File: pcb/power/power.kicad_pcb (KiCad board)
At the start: 4 copper layers, 100 x 100 mm, 34 parts, among them J101 XT30PW-M, J102 Conn_02x10_Row_Letter_First, U201 TPS62933, U301 INA226, U401 INA226

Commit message: update ALL parts
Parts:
- C102, C103: footprint Capacitor_Tantalum_SMD:CP_EIA-7343-43_Kemet-X_Pad2.25x2.55mm_HandSolder -> Capacitor_Tantalum_SMD:CP_EIA-7343-43_Kemet-X
- C301, C401: value 100nF -> 100n
- R101: value 1k8 -> 2k2
- R102: value 360 -> 1k

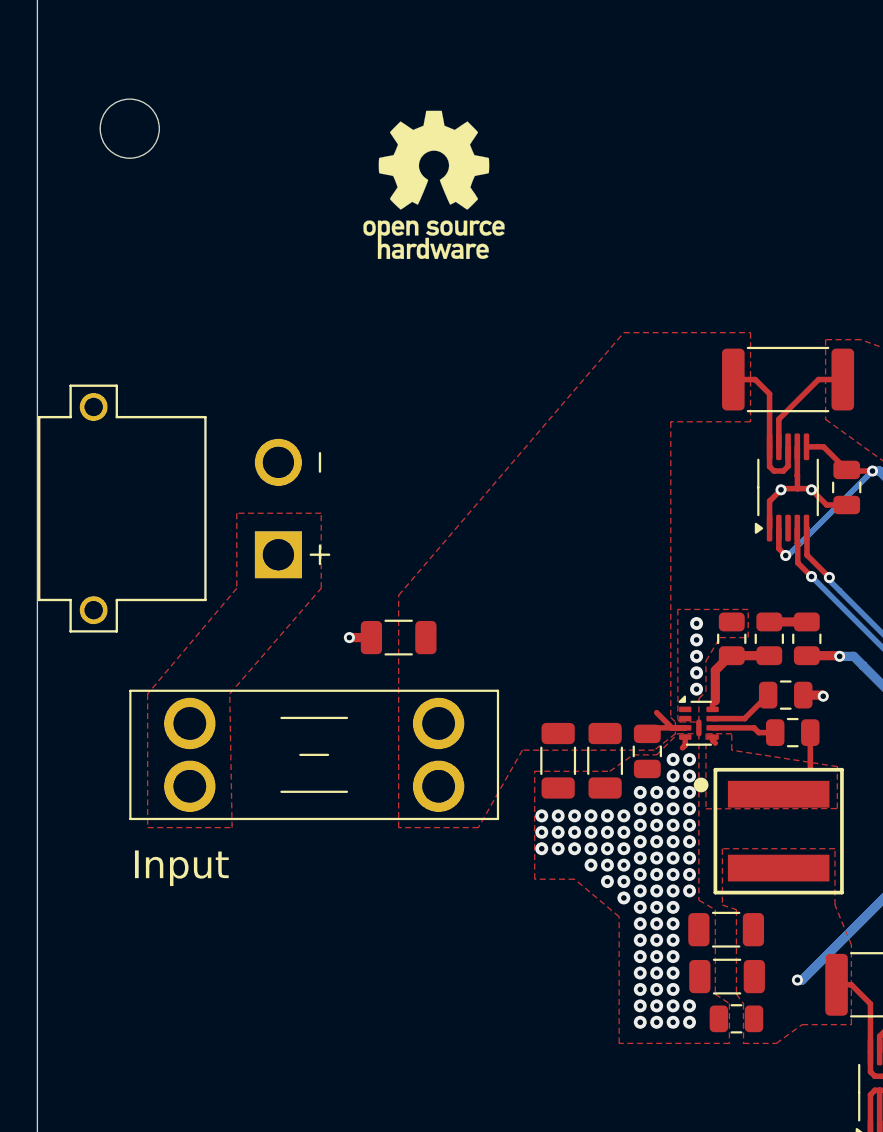
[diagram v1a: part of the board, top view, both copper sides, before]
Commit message: update XT30 to XT60 connector
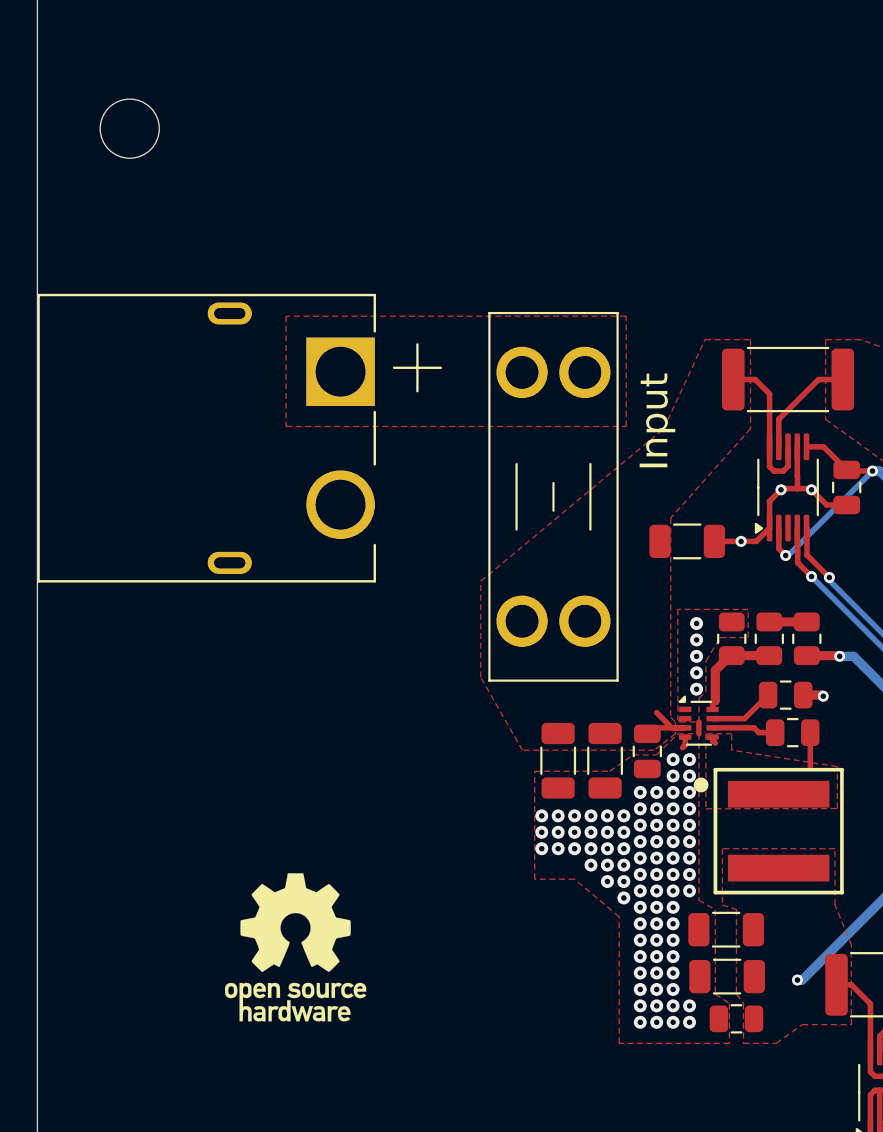
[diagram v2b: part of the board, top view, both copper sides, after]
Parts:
- J101: value XT30PW-M -> XT60PW-M; footprint PRJ:XT30PW-M -> PRJ:AMASS_XT60PW-M
- moved #SYM101 41.9 mm to (113.5, 92.5)
- moved F101 19.1 mm to (127.5, 68.1), turned to -90 degrees
- moved C101 16.5 mm to (134.7, 70.5), turned to 0 degrees
- moved J101 8.29 mm to (110.0, 64.9)
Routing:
- net GND: track 27.8 -> 29.9 mm

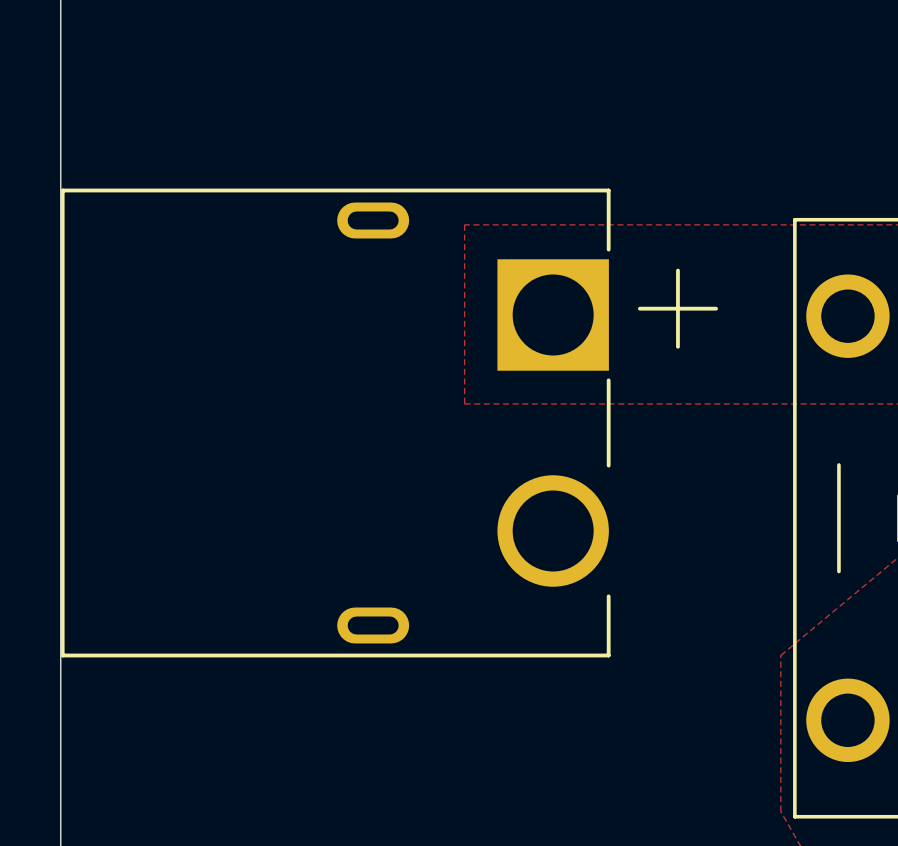
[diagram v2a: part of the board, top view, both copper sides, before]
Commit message: update XT60 connector to official one
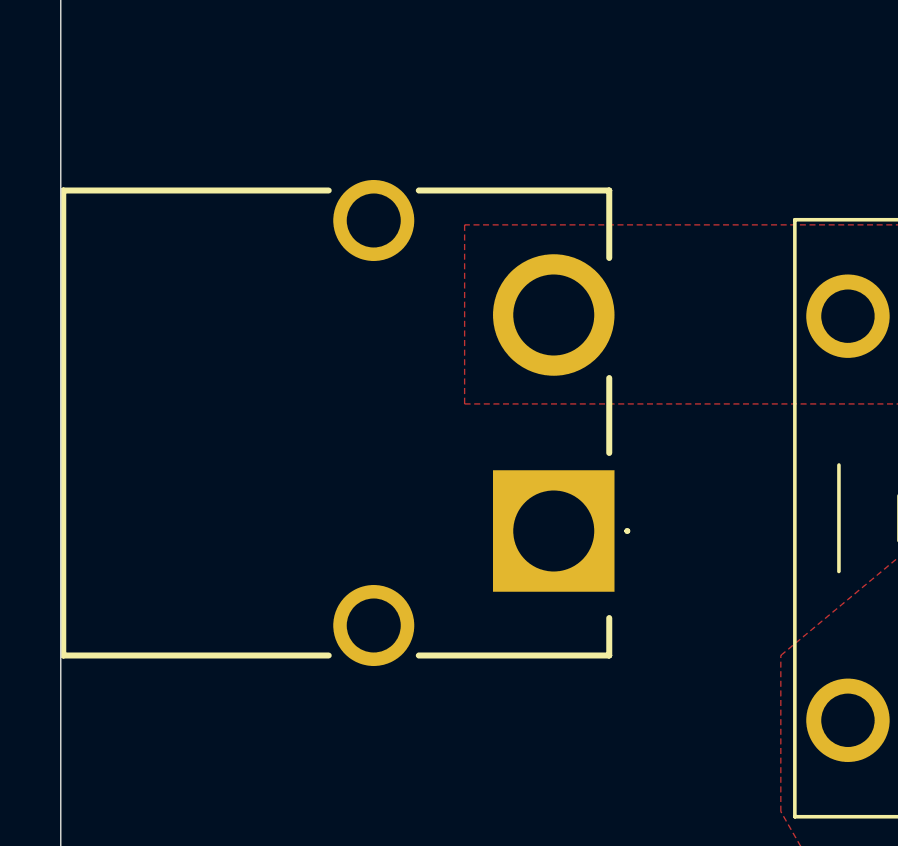
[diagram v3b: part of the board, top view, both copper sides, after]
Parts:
- J101: footprint PRJ:AMASS_XT60PW-M -> PRJ:XT60PWM
- moved J101 7.01 mm to (116.0, 68.5)
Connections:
- J101 pad 1: /12V_IN_UNPROTECTED -> GND
- J101 pad 2: GND -> /12V_IN_UNPROTECTED

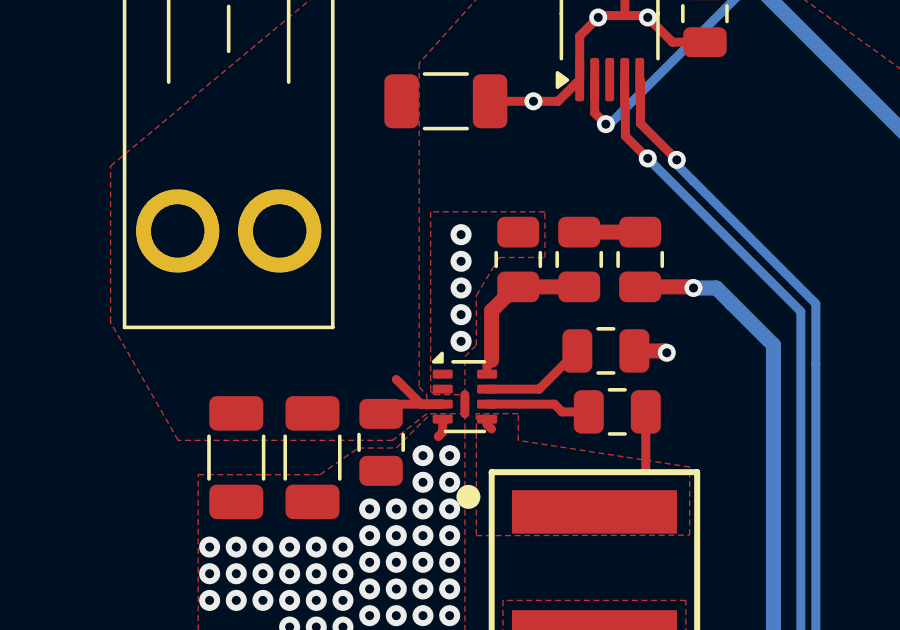
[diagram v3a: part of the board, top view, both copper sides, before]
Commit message: fix power, pin 2
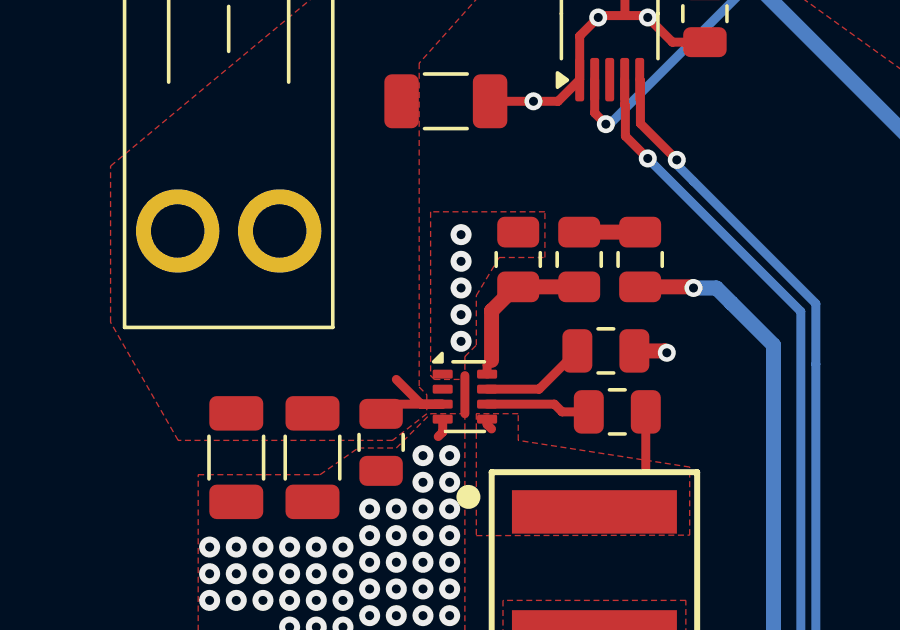
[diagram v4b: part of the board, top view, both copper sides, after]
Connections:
- U201 pad 2: GND -> unconnected-(U201-EN-Pad2)
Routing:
- net GND: track 29.9 -> 30.5 mm
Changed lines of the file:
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@@
 	(net 24 "Net-(U201-BST)")
 	(net 25 "/12V_IN_UNPROTECTED")
+	(net 26 "unconnected-(U201-EN-Pad2)")
 	(footprint "PRJ:Fuseholder"
 		(layer "F.Cu")
@@
 			(layers "F.Cu" "F.Mask" "F.Paste")
 			(roundrect_rratio 0.1666666667)
-			(net 1 "GND")
+			(net 26 "unconnected-(U201-EN-Pad2)")
 			(pinfunction "EN")
-			(pintype "input")
+			(pintype "input+no_connect")
 			(thermal_bridge_angle 45)
 		)
@@
 	)
 	(segment
+		(start 135.382 79.629)
+		(end 135.382 80.899)
+		(width 0.3)
+		(layer "F.Cu")
+		(net 1)
+	)
+	(segment
 		(start 162.99 76.376)
 		(end 164.24 76.376)
@@
 	)
 	(segment
-		(start 135.382 80.264)
-		(end 135.382 80.899)
-		(width 0.3)
-		(layer "F.Cu")
-		(net 1)
-	)
-	(segment
 		(start 140.708 66.921)
 		(end 140.716 66.929)
@@
 		(polygon
 			(pts
-				(xy 134.366 80.264) (xy 135.382 80.264) (xy 135.382 78.994) (xy 135.763 78.613) (xy 135.763 76.962)
-				(xy 136.525 75.692) (xy 138.049 75.692) (xy 138.049 74.168) (xy 134.239 74.168) (xy 134.241886 80.142772)
+				(xy 134.366 79.756) (xy 135.382 79.756) (xy 135.382 78.994) (xy 135.763 78.613) (xy 135.763 76.962)
+				(xy 136.525 75.692) (xy 138.049 75.692) (xy 138.049 74.168) (xy 134.239 74.168) (xy 134.239 79.629)
 			)
 		)

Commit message: update power pcb
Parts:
- removed C204: 33n, Capacitor_SMD:C_0805_2012Metric
- removed U201: TPS62933, Package_TO_SOT_SMD:SOT-583-8
- added C104: 100u / 25V, Capacitor_Tantalum_SMD:CP_EIA-7343-43_Kemet-X, F.Cu at (144.8, 86.1)
- added U203: LMR51430 500kHz, Package_TO_SOT_SMD:SOT-23-6, F.Cu at (146.6, 98.7)
- F101, F102, F103: footprint PRJ:Fuseholder -> PRJ:FUSE_01530007Z
- R202: value 53k6 -> 100k
- R203: value 10k2 -> 13k7
- R301, R401: value 100m -> 10m
- moved F102 68.0 mm to (104.2, 99.3), turned to -90 degrees
- moved F103 66.4 mm to (104.2, 118.1), turned to -90 degrees
- moved D101 52.5 mm to (122.4, 100.3), turned to 180 degrees
- moved D102 50.9 mm to (122.4, 119.1), turned to 180 degrees
- moved #SYM101 49.1 mm to (162.4, 88.4)
- moved R101 48.0 mm to (122.4, 98.2)
- moved R102 46.4 mm to (122.4, 117.0)
- moved U401 31.3 mm to (128.4, 96.5)
- moved R401 31.3 mm to (128.4, 90.7), turned to 180 degrees
- moved C401 30.5 mm to (131.4, 95.6)
- moved F101 26.4 mm to (104.2, 80.5)
- moved R203 24.4 mm to (142.0, 99.7), turned to 180 degrees
- moved C205 23.3 mm to (147.2, 103.1)
- moved L201 23.1 mm to (152.9, 105.2)
- moved C301 23.0 mm to (131.3, 114.2)
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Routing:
- net /5V: track 92.9 -> 59.6 mm, vias 3 -> 2
- net /I2C_SDA1: track 89.5 -> 98.8 mm
- net /12V_IN: track 12.6 -> 21.1 mm, vias 0 -> 2
- net /5V_IN: track 31.3 -> 39.4 mm
- net GND: track 30.5 -> 36.8 mm, vias 103 -> 25
- net /12V: track 16.1 -> 21.0 mm
- net /I2C_SCL1: track 93.9 -> 98.3 mm, vias 2 -> 4
- net Net-(U201-SS): track 3.54 -> 0.00 mm
- net Net-(U203-CB): track 3.50 -> 6.37 mm, vias 0 -> 2
- net /5V/TPS_SW: track 2.29 -> 1.57 mm
- added copper zone on B.Cu, net /12V
- added copper zone on B.Cu, net /5V
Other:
- board text added: "12V Fuse"
- board text added: "5V Fuse"
- board text added: "Input Fuse"
- board text removed: "12V"
- board text removed: "5V"
- board text removed: "Input"

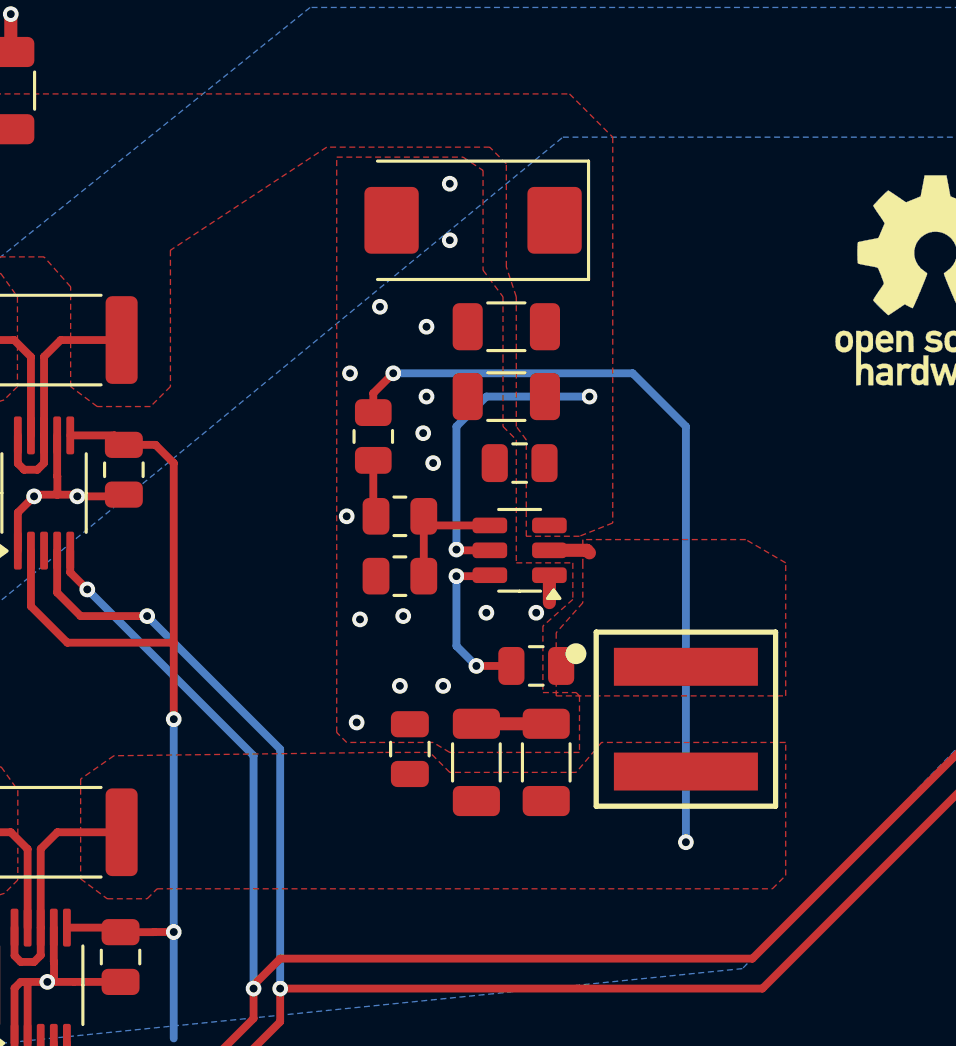
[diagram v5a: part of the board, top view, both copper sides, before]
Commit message: update fields and mouser components
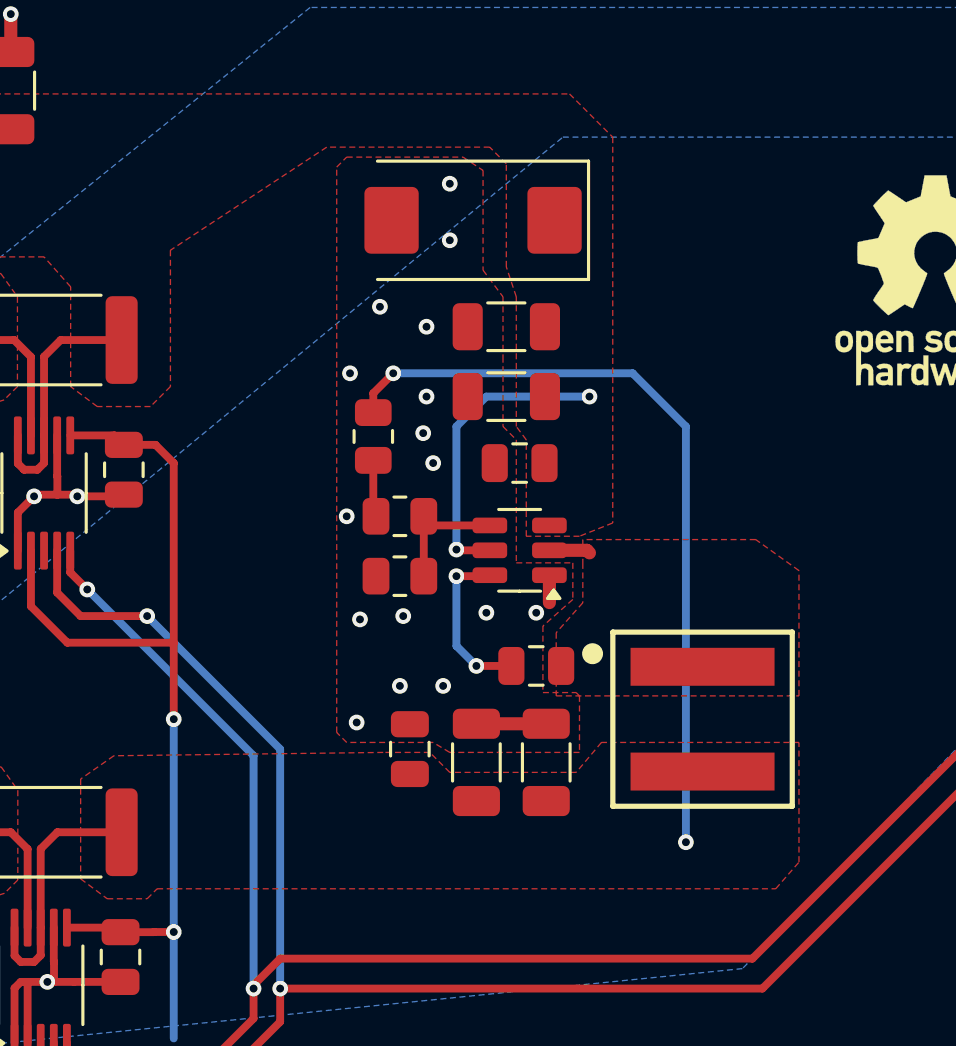
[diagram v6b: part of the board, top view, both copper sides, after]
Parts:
- moved L201 0.64 mm to (153.5, 105.2)
